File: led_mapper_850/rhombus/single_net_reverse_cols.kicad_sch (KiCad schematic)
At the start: 529 parts

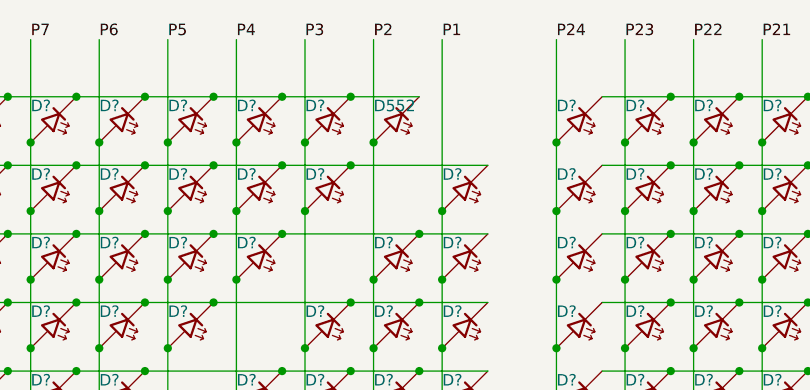
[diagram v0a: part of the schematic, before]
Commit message: Sync changes: update holes to 2.2mm, change footprint to match datasheet
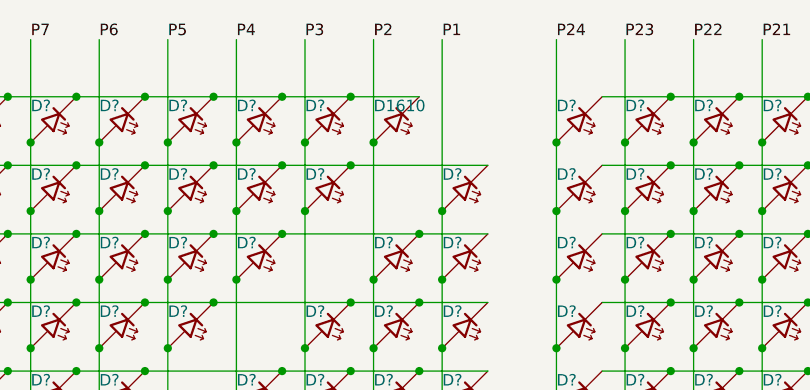
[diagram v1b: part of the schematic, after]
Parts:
- D1610: renamed from D552; footprint LED_SMD:LED_0201_0603Metric -> ccatlib:LED_0201_0603Metric_XINGLIGHT
- D? (x528): footprint LED_SMD:LED_0201_0603Metric -> ccatlib:LED_0201_0603Metric_XINGLIGHT
